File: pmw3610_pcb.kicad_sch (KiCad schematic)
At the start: 15 parts, among them J1 Conn_01x02, J2 Conn_01x04, U1 PMW3610, U2 TLV74318PDBVR

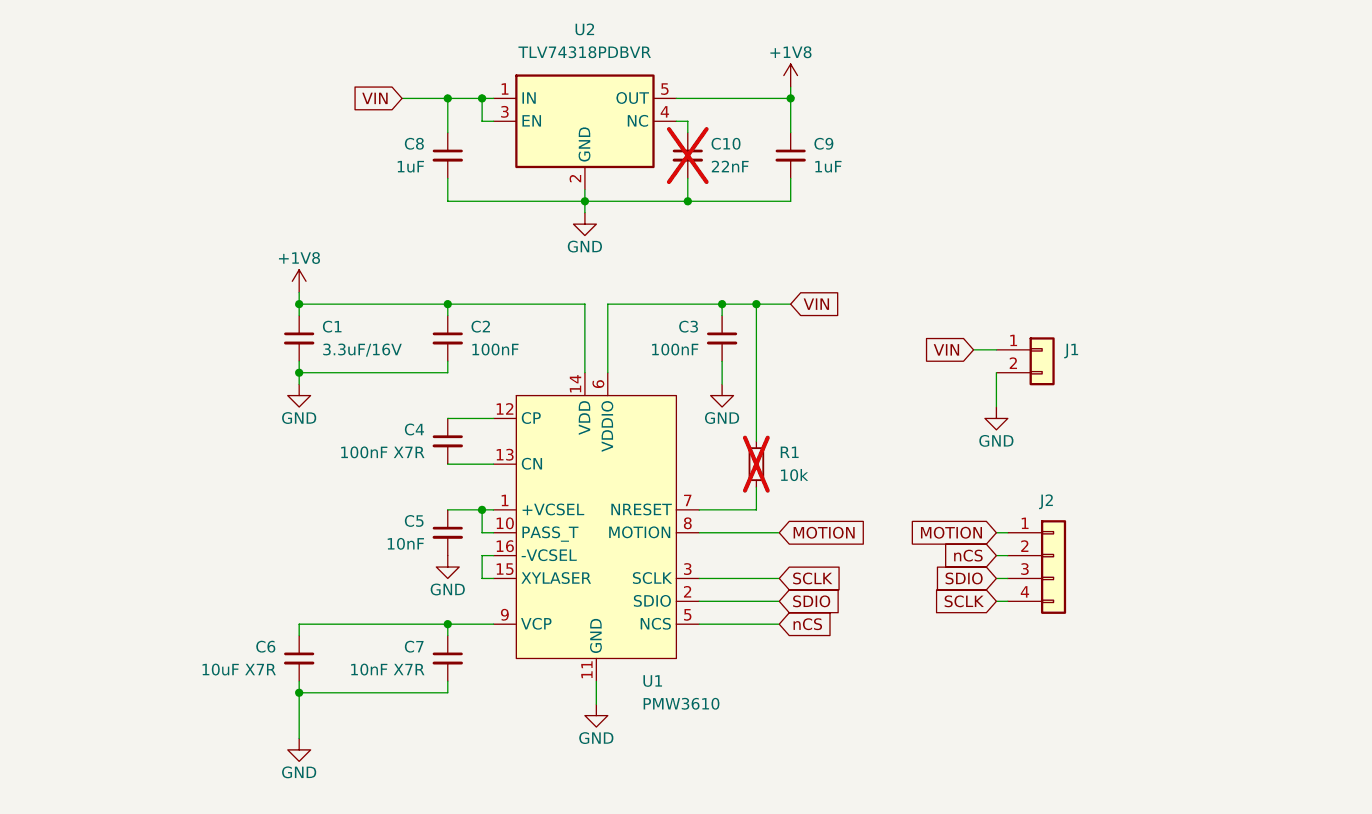
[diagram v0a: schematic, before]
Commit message: modify size (25mm x 22mm)
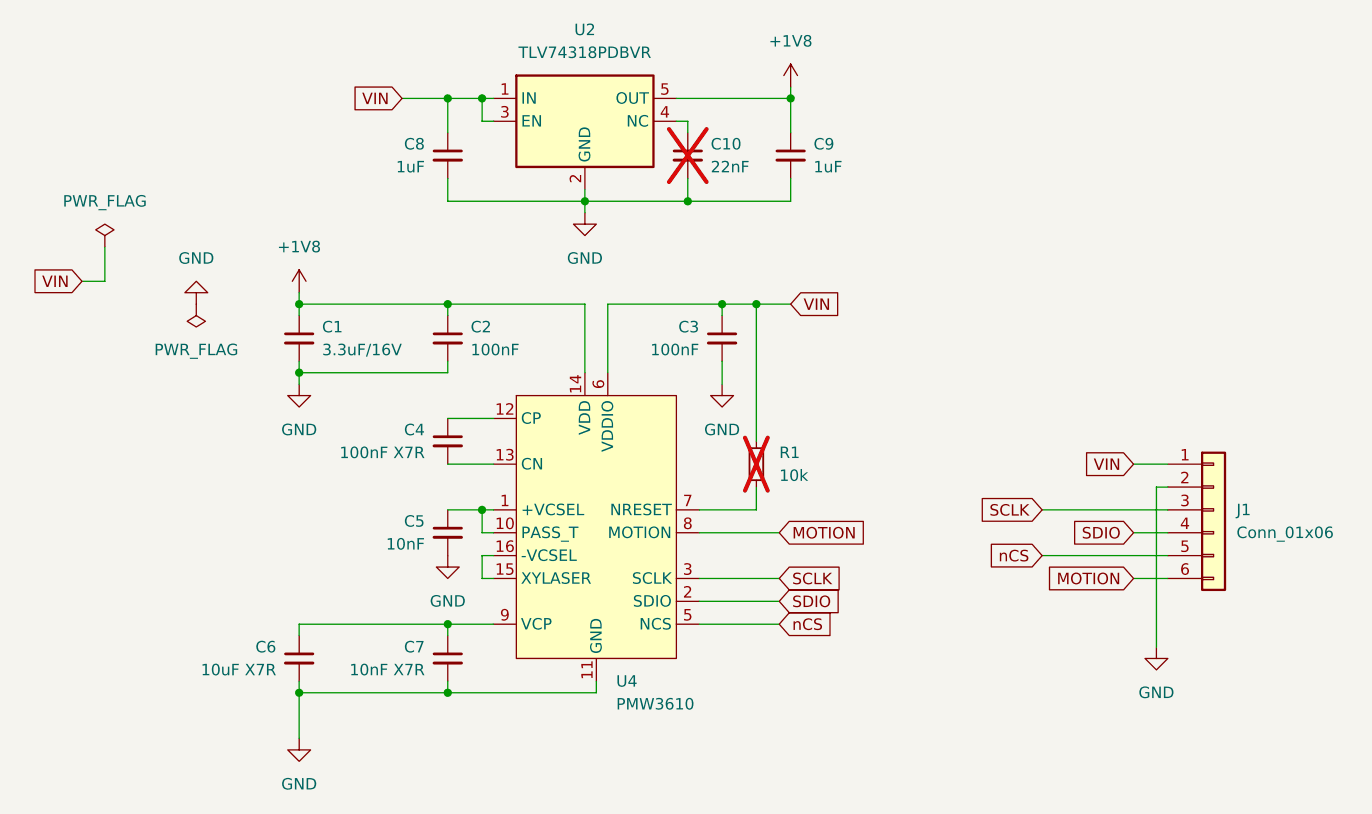
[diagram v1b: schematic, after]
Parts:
- removed J1: Conn_01x02, Connector_PinHeader_2.54mm:PinHeader_1x02_P2.54mm_Vertical, symbol Connector_Generic:Conn_01x02
- removed J2: Conn_01x04, Connector_PinHeader_2.54mm:PinHeader_1x04_P2.54mm_Vertical, symbol Connector_Generic:Conn_01x04
- removed U1: PMW3610, pmw3610_pcb:PMW3610DM-SUDU 16Pin, symbol pmw3610_pcb:PMW3610DM-SUDU
- added J1: Conn_01x06, Connector_PinHeader_2.54mm:PinHeader_1x06_P2.54mm_Vertical, symbol Connector_Generic:Conn_01x06
- added U4: PMW3610, pmw3610_pcb:PMW3610DM-SUDU 16Pin, symbol pmw3610_pcb:PMW3610DM-SUDU
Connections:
- net +1V8: now also U4.14 (VDD)
- net GND: now also J1.2 (Pin_2), U4.11 (GND)
- net MOTION: now also J1.6 (Pin_6), U4.8 (MOTION)
- net SCLK: now also J1.3 (Pin_3), U4.3 (SCLK)
- net SDIO: now also J1.4 (Pin_4), U4.2 (SDIO)
- net VIN: now also J1.1 (Pin_1), U4.6 (VDDIO)
- net nCS: now also J1.5 (Pin_5), U4.5 (NCS)
- net at C5.1: now also U4.1 (+VCSEL), U4.10 (PASS_T)
- net at C4.1: now also U4.12 (CP)
- net at C4.2: now also U4.13 (CN)
- net at R1.2: now also U4.7 (NRESET)
- net at C6.1, C7.1: now also U4.9 (VCP)
- new net: U4.15 (XYLASER), U4.16 (-VCSEL)

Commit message: [jlcpcb] Add order files
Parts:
- J1: now left out of the parts list
- U4: now not fitted; now left out of the parts list
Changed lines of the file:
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@@
 		(unit 1)
 		(exclude_from_sim no)
-		(in_bom yes)
-		(on_board yes)
+		(in_bom no)
+		(on_board no)
 		(dnp no)
 		(fields_autoplaced yes)
@@
 		(unit 1)
 		(exclude_from_sim no)
-		(in_bom yes)
-		(on_board yes)
-		(dnp no)
+		(in_bom no)
+		(on_board yes)
+		(dnp yes)
 		(fields_autoplaced yes)
 		(property "Reference" "U4"
